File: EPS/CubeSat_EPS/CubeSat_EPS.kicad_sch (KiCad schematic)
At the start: 32 parts, among them J1 SOLAR_IN, J10 AUX_POWER_OUT, J11 INA226_MODULE, J12 ADCS_5V_POWER, J2 CN3722_2S_MPPT_MODULE, J3 BMS_MODULE, J4 BATTERY_PACK, J5 BUCK_5V_MODULE, J6 OBC_INTERFACE, J7 BUCK_3V3_MODULE, J8 ADCS_POWER, J9 TTC_POWER, Q1 P-MOSFET

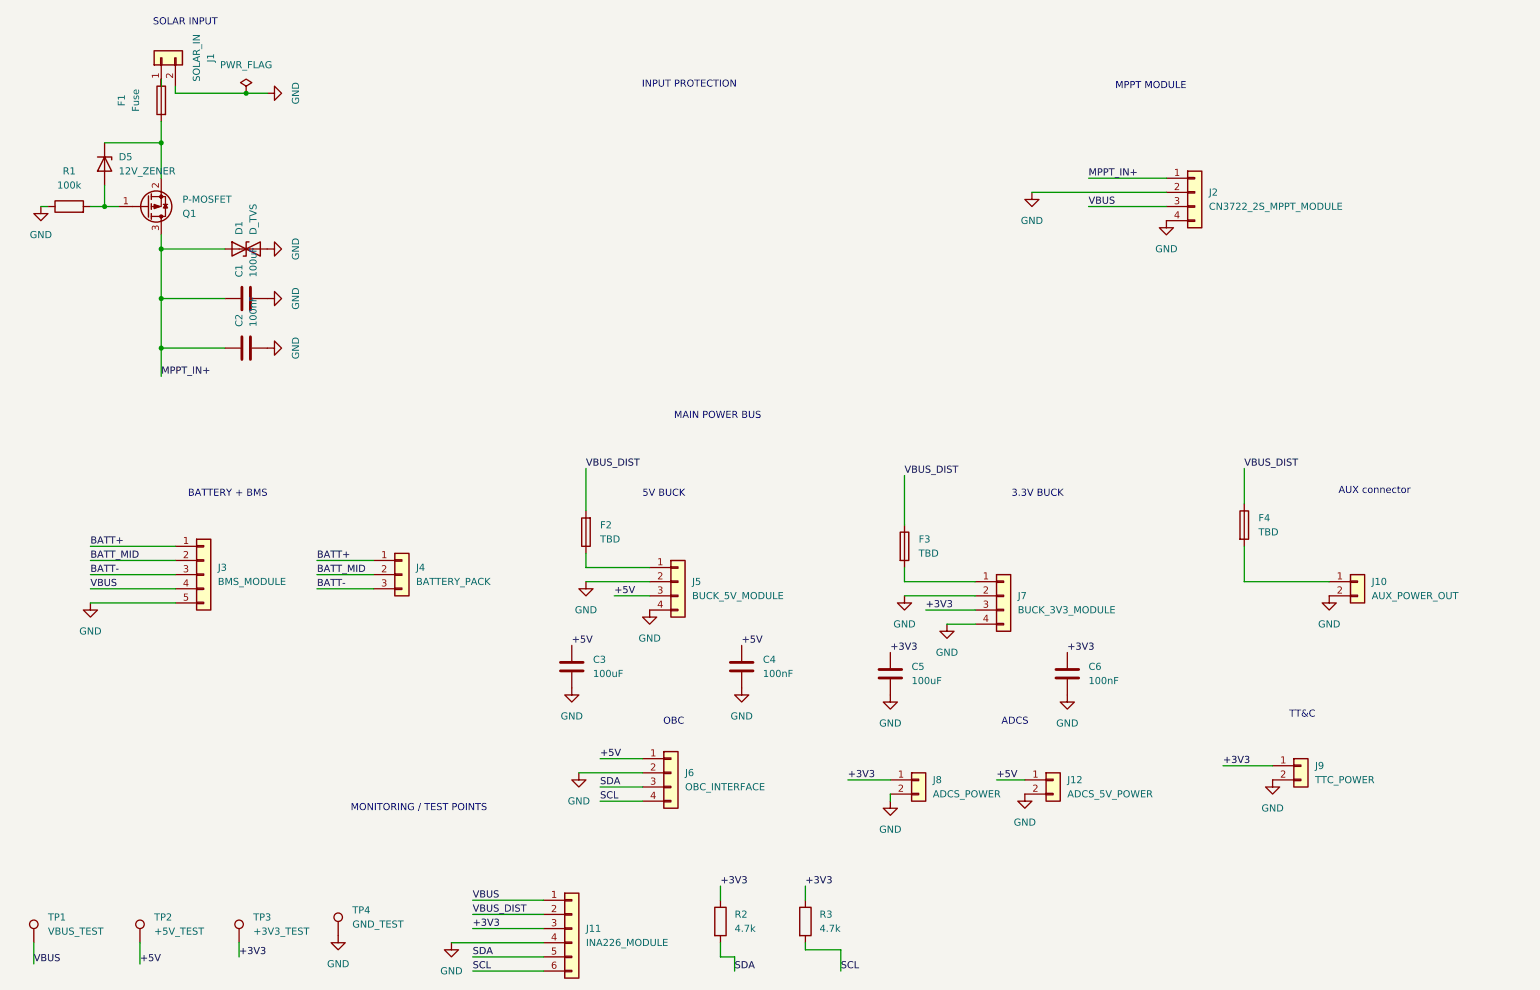
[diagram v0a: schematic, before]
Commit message: Fix: Move EPS files to correct folder (EPS/CubeSat_EPS/)
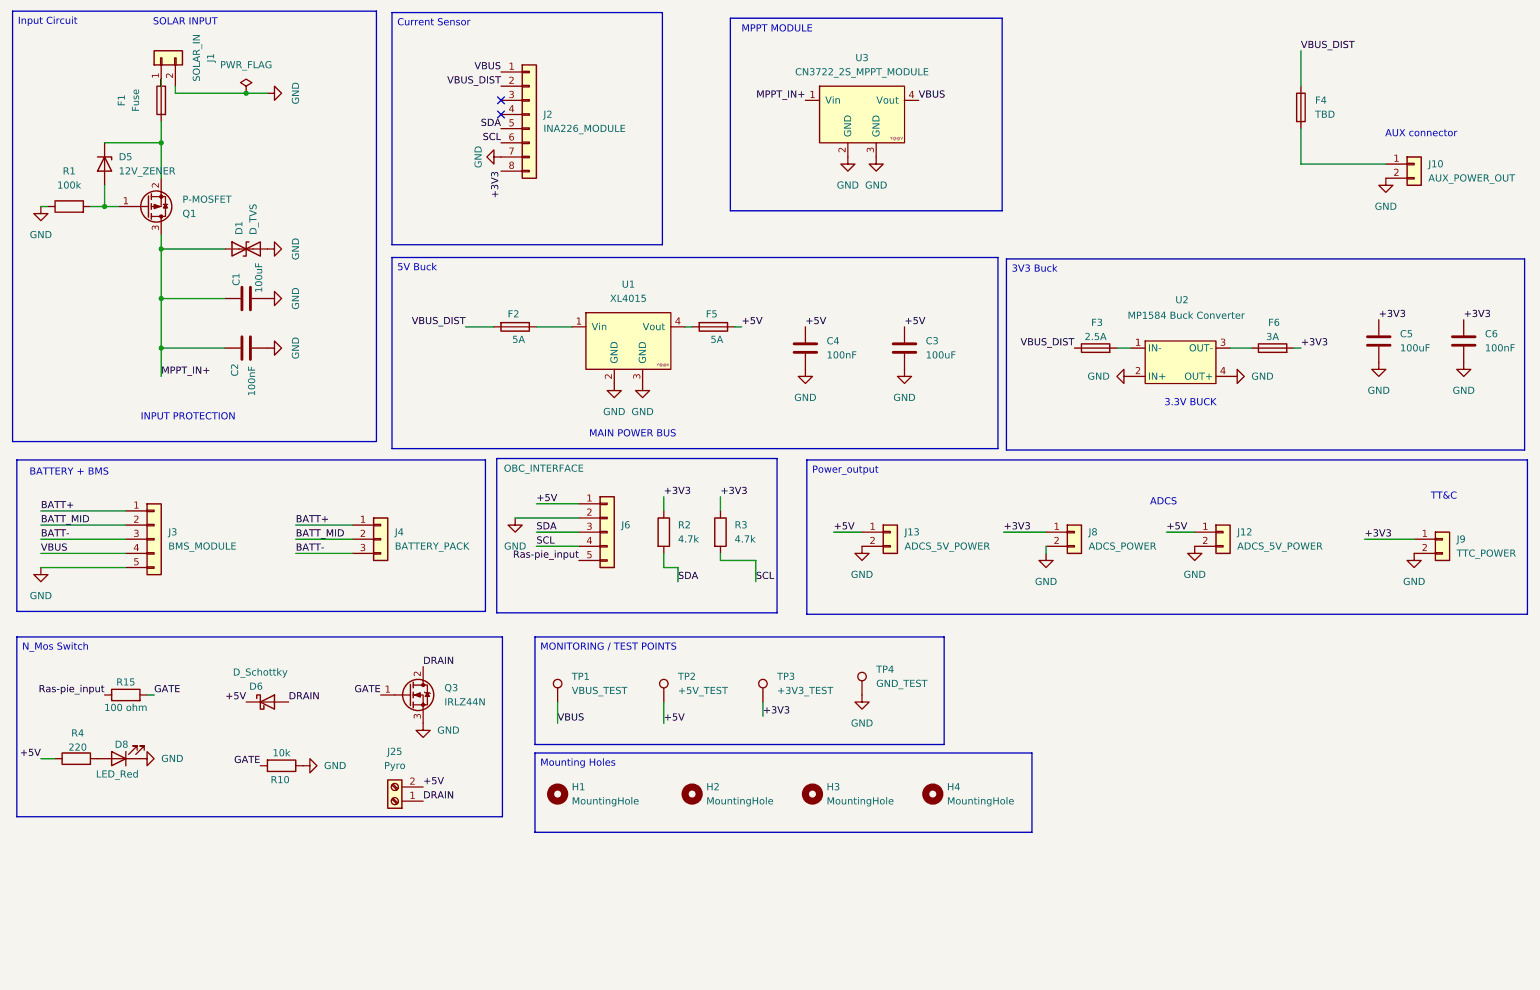
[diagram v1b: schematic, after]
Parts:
- removed J11: INA226_MODULE, Connector_PinHeader_2.54mm:PinHeader_1x06_P2.54mm_Vertical, symbol Connector_Generic:Conn_01x06
- removed J2: CN3722_2S_MPPT_MODULE, Connector_PinHeader_2.54mm:PinHeader_1x04_P2.54mm_Vertical, symbol Connector_Generic:Conn_01x04
- removed J5: BUCK_5V_MODULE, Connector_PinHeader_2.54mm:PinHeader_1x04_P2.54mm_Vertical, symbol Connector_Generic:Conn_01x04
- removed J7: BUCK_3V3_MODULE, Connector_PinHeader_2.54mm:PinHeader_1x04_P2.54mm_Vertical, symbol Connector_Generic:Conn_01x04
- added D6: D_Schottky, Diode_SMD:D_SMA, symbol Device:D_Schottky
- added D8: LED_Red, LED_SMD:LED_0805_2012Metric_Pad1.15x1.40mm_HandSolder, symbol Device:LED
- added F5: 5A, Fuse:Fuse_1206_3216Metric, symbol Device:Fuse
- added F6: 3A, Fuse:Fuse_1206_3216Metric, symbol Device:Fuse
- added H1, H2, H3, H4: MountingHole, MountingHole:MountingHole_4.3mm_M4, symbol Mechanical:MountingHole
- added J13: ADCS_5V_POWER, Connector_JST:JST_VH_B2P-VH-B_1x02_P3.96mm_Vertical, symbol Connector_Generic:Conn_01x02
- added J2: INA226_MODULE, 815-2:INA226 Current Sensor, symbol Connector_Generic:Conn_01x08
- added J25: Pyro, TerminalBlock_TE-Connectivity:TerminalBlock_TE_282834-2_1x02_P2.54mm_Horizontal, symbol Connector:Screw_Terminal_01x02
- added Q3: IRLZ44N, Package_TO_SOT_THT:TO-220-3_Vertical, symbol Transistor_FET:IRLZ44N
- added R10: 10k, Resistor_SMD:R_0805_2012Metric_Pad1.20x1.40mm_HandSolder, symbol Device:R
- added R15: 100 ohm, Resistor_SMD:R_0805_2012Metric_Pad1.20x1.40mm_HandSolder, symbol Device:R
- added R4: 220, Resistor_SMD:R_0805_2012Metric_Pad1.20x1.40mm_HandSolder, symbol Device:R
- added U1: XL4015, 815-2:XL4015 Buck, symbol yaaj_dcdc_stepdown_lm2596:YAAJ_DCDC_StepDown_LM2596
- added U2: MP1584 Buck Converter, MP1584:MP1584 module 20mm_15mm, symbol MP1584:MP1584_Buck_converter
- added U3: CN3722_2S_MPPT_MODULE, 815-2:MPPT Solar, symbol yaaj_dcdc_stepdown_lm2596:YAAJ_DCDC_StepDown_LM2596
- C1, C3, C5: footprint Capacitor_THT:CP_Radial_D6.3mm_P2.50mm -> Capacitor_SMD:C_0805_2012Metric_Pad1.18x1.45mm_HandSolder
- D1: footprint Diode_THT:D_DO-41_SOD81_P10.16mm_Horizontal -> Diode_SMD:D_SOD-123
- D5: footprint Diode_THT:D_DO-41_SOD81_P10.16mm_Horizontal -> Diode_SMD:D_SMA
- F2: value TBD -> 5A
- F3: value TBD -> 2.5A
- J6: footprint Connector_JST:JST_VH_B4P-VH_1x04_P3.96mm_Vertical -> Connector_JST:JST_VH_B5P-VH_1x05_P3.96mm_Vertical; symbol Connector_Generic:Conn_01x04 -> Connector_Generic:Conn_01x05
- TP1: footprint TestPoint:TestPoint_Plated_Hole_D2.0mm -> TestPoint:TestPoint_Pad_D1.5mm
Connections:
- net +3V3: now also F6.2, J2.8 (Pin_8)
- net +5V: now also D6.1 (K), F5.1, J13.1 (Pin_1), J25.2 (Pin_2), R4.1
- net GND: now also D8.1 (K), J13.2 (Pin_2), J2.7 (Pin_7), Q3.3 (S), R10.1, U1.2 (GND), U1.3 (GND), U2.2 (IN+), U2.4 (OUT+), U3.2 (GND), U3.3 (GND)
- net MPPT_IN+: now also U3.1 (Vin)
- net SCL: now also J2.6 (Pin_6)
- net SDA: now also J2.5 (Pin_5)
- net VBUS: now also J2.1 (Pin_1), U3.4 (Vout)
- net VBUS_DIST: now also J2.2 (Pin_2)
- net at F3.2: now also U2.1 (IN-)
- net at F2.1: now also U1.1 (Vin)
- new net: F6.1, U2.3 (OUT-)
- new net: D8.2 (A), R4.2
- new net: F5.2, U1.4 (Vout)
- new net DRAIN: D6.2 (A), J25.1 (Pin_1), Q3.2 (D)
- new net GATE: Q3.1 (G), R10.2, R15.2
- new net Ras-pie_input: J6.5 (Pin_5), R15.1
- no-connect marks 0 -> 2
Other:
- note removed: "5V BUCK"
- note removed: "MONITORING / TEST POINTS"
- note removed: "OBC"
- moved on the sheet: C3, C4, C5, C6, F4, J10, J12, J3, J4, J8, J9, R2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
